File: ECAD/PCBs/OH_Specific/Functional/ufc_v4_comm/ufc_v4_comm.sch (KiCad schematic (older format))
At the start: 18 parts, among them J1 Conn_01x05_Male, J2 Conn_01x05_Male

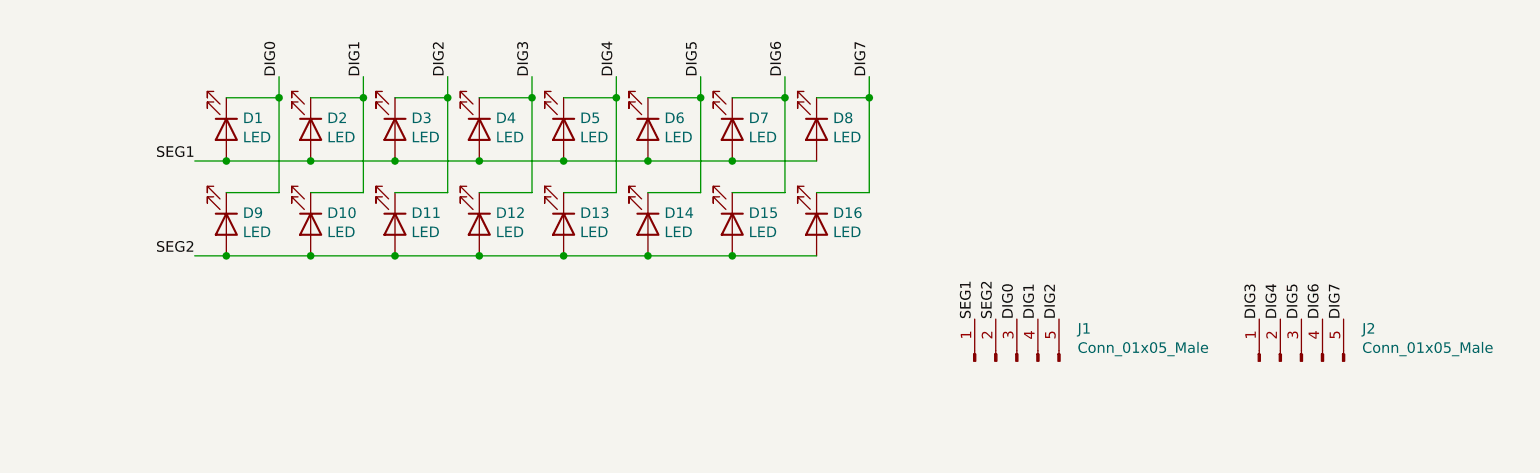
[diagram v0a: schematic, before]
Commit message: Modified scratchpad: 16 segment display rerouted to follow the same configuration as OPT. minor cleaning on the 7 segment displays updated .gitignore to ignore the rescue files.
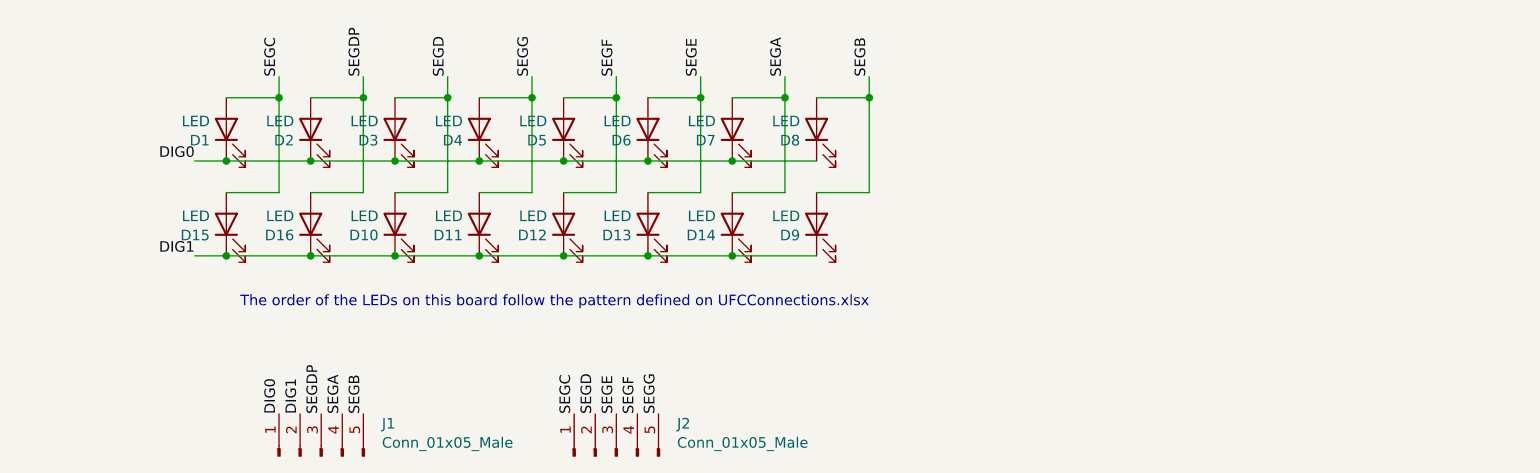
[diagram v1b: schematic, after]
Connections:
- net DIG0: now also D2.1 (K), D3.1 (K), D4.1 (K), D5.1 (K), D6.1 (K), D7.1 (K), D8.1 (K), J1.1 (Pin_1); no longer D9.1 (K), J1.3 (Pin_3)
- net DIG1: now also D11.1 (K), D12.1 (K), D13.1 (K), D14.1 (K), D15.1 (K), D16.1 (K), D9.1 (K), J1.2 (Pin_2); no longer D2.1 (K), J1.4 (Pin_4)
- removed net DIG2: D11.1 (K), D3.1 (K), J1.5 (Pin_5)
- removed net DIG3: D12.1 (K), D4.1 (K), J2.1 (Pin_1)
- removed net DIG4: D13.1 (K), D5.1 (K), J2.2 (Pin_2)
- removed net DIG5: D14.1 (K), D6.1 (K), J2.3 (Pin_3)
- removed net DIG6: D15.1 (K), D7.1 (K), J2.4 (Pin_4)
- removed net DIG7: D16.1 (K), D8.1 (K), J2.5 (Pin_5)
- removed net SEG1: D1.2 (A), D2.2 (A), D3.2 (A), D4.2 (A), D5.2 (A), D6.2 (A), D7.2 (A), D8.2 (A), J1.1 (Pin_1)
- removed net SEG2: D10.2 (A), D11.2 (A), D12.2 (A), D13.2 (A), D14.2 (A), D15.2 (A), D16.2 (A), D9.2 (A), J1.2 (Pin_2)
- new net SEGA: D14.2 (A), D7.2 (A), J1.4 (Pin_4)
- new net SEGB: D8.2 (A), D9.2 (A), J1.5 (Pin_5)
- new net SEGC: D1.2 (A), D15.2 (A), J2.1 (Pin_1)
- new net SEGD: D10.2 (A), D3.2 (A), J2.2 (Pin_2)
- new net SEGDP: D16.2 (A), D2.2 (A), J1.3 (Pin_3)
- new net SEGE: D13.2 (A), D6.2 (A), J2.3 (Pin_3)
- new net SEGF: D12.2 (A), D5.2 (A), J2.4 (Pin_4)
- new net SEGG: D11.2 (A), D4.2 (A), J2.5 (Pin_5)
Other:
- note added: "The order of the LEDs on this board follow the pattern defined on UFCConnections.xlsx"
- moved on the sheet: D1, D10, D11, D12, D13, D14, D15, D16, D2, D3, D4, D5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
